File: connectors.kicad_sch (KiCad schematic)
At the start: 9 parts, among them J1 PRT-14417, J6 10152803-00011LF, J9 Conn_01x02, P1 TC2050-IDC

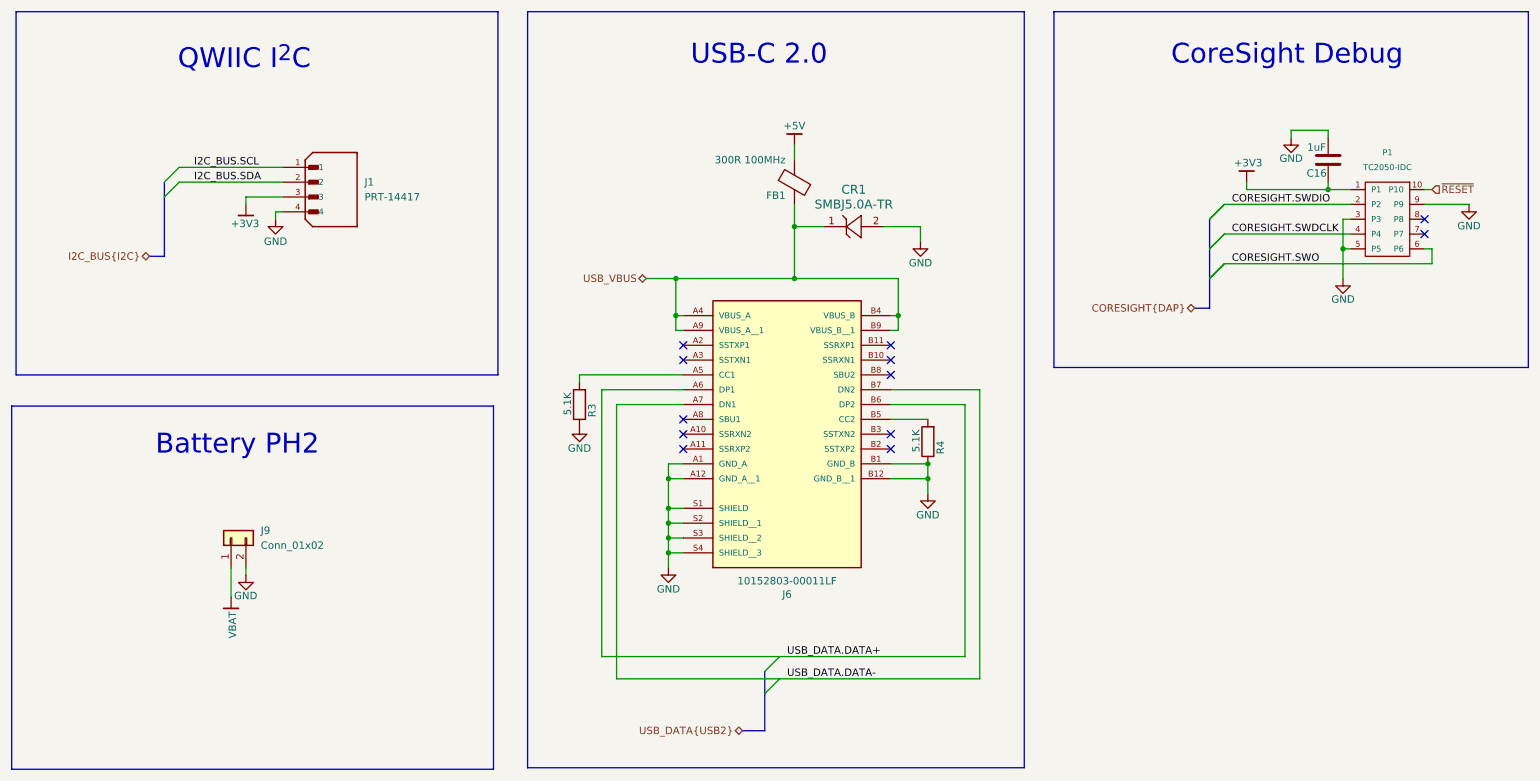
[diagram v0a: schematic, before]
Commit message: Release candidate
Changed USBC connector, changed TagConnect to use footprint with legs, move NRF52 to edge of board, clean up traces
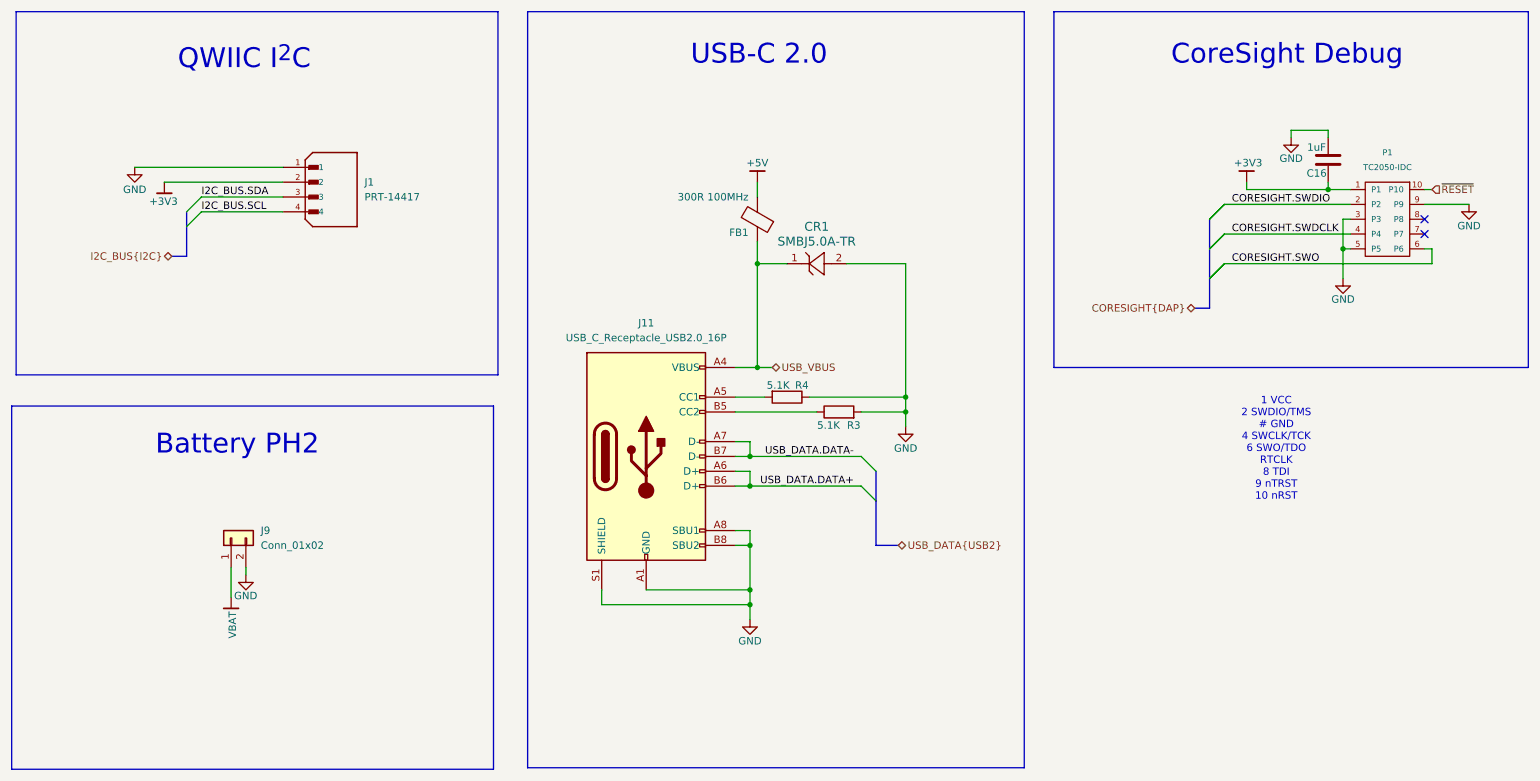
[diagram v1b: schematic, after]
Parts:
- removed J6: 10152803-00011LF, 10152803_00011LF:AMPHENOL_10152803-00011LF, symbol 10152803-00011LF:10152803-00011LF
- added J11: USB_C_Receptacle_USB2.0_16P, Connector_USB:USB_C_Receptacle_GCT_USB4105-xx-A_16P_TopMnt_Horizontal, symbol Connector:USB_C_Receptacle_USB2.0_16P
- P1: footprint Connector:Tag-Connect_TC2050-IDC-NL_2x05_P1.27mm_Vertical -> Connector:Tag-Connect_TC2050-IDC-FP_2x05_P1.27mm_Vertical
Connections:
- net +3V3: now also J1.2; no longer J1.3
- net GND: now also J1.1, R3.2, J11.A1 (GND), J11.A12 (GND), J11.A8 (SBU1), J11.B1 (GND), J11.B12 (GND), J11.B8 (SBU2), J11.S1 (SHIELD); no longer J1.4, R3.1
- net I2C_BUS.SCL: now also J1.4; no longer J1.1
- net I2C_BUS.SDA: now also J1.3; no longer J1.2
- net USB_DATA.DATA+: now also J11.A6 (D+), J11.B6 (D+)
- net USB_DATA.DATA-: now also J11.A7 (D-), J11.B7 (D-)
- net USB_VBUS: now also J11.A4 (VBUS), J11.A9 (VBUS), J11.B4 (VBUS), J11.B9 (VBUS)
- net at R4.2: now also J11.A5 (CC1)
- new net: J11.B5 (CC2), R3.1
- no-connect marks 12 -> 2
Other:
- note added: "1 VCC 2 SWDIO/TMS # GND 4 SWCLK/TCK 6 SWO/TDO RTCLK 8 TDI 9 nTRST 10 nRST"
- moved on the sheet: CR1, FB1, R3, R4

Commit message: Update part numbers
Update part numbers for 12 and 16 PIN SMD 2.54mm pins and USB-C 2.0 connector.
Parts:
- J11: MP (none) -> USB4105-GF-A
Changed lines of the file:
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@@
+			)
+		)
+		(property "MP" "USB4105-GF-A"
+			(at 128.27 93.98 0)
+			(effects
+				(font
+					(size 1.27 1.27)
+				)
+				(hide yes)
 			)
 		)

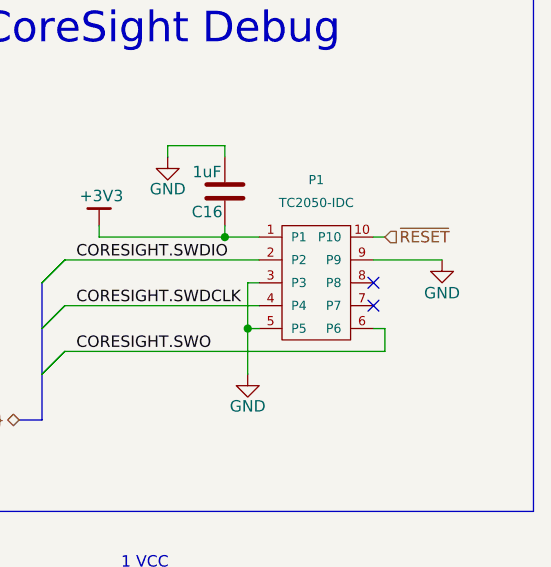
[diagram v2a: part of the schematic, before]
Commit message: Tweak locations and add a bypass capacitor for VBUS
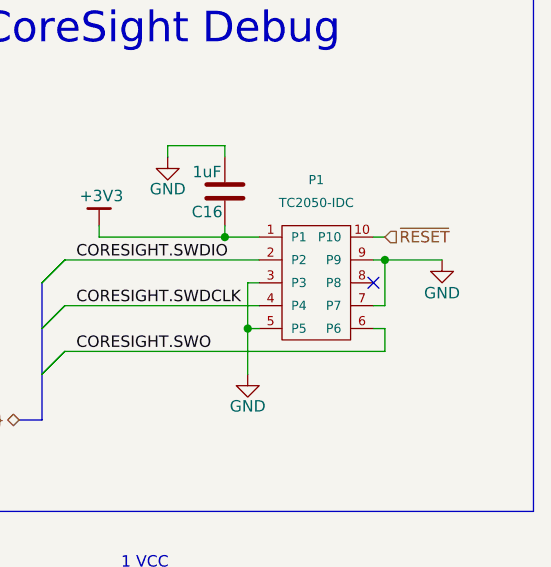
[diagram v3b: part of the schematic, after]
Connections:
- net GND: now also P1.7 (P7)
- no-connect marks 2 -> 1
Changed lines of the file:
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@@
+		(color 0 0 0 0)
+	)
+	(junction
+		(at 262.89 50.8)
+		(diameter 0)
 		(color 0 0 0 0)
 	)
@@
 		(at 261.62 53.34)
 	)
-	(no_connect
-		(at 261.62 55.88)
-	)
 	(bus_entry
 		(at 167.64 96.52)
@@
 	(wire
 		(pts
+			(xy 261.62 55.88) (xy 262.89 55.88)
+		)
+		(stroke
+			(width 0)
+			(type default)
+		)
+	)
+	(wire
+		(pts
 			(xy 231.14 48.26) (xy 231.14 46.99)
 		)
@@
 	(wire
 		(pts
+			(xy 262.89 50.8) (xy 261.62 50.8)
+		)
+		(stroke
+			(width 0)
+			(type default)
+		)
+	)
+	(wire
+		(pts
 			(xy 143.51 93.98) (xy 146.05 93.98)
 		)
@@
 	(wire
 		(pts
+			(xy 262.89 50.8) (xy 262.89 55.88)
+		)
+		(stroke
+			(width 0)
+			(type default)
+		)
+	)
+	(wire
+		(pts
 			(xy 245.11 48.26) (xy 248.92 48.26)
 		)
@@
 	(wire
 		(pts
-			(xy 269.24 50.8) (xy 261.62 50.8)
-		)
-		(stroke
+			(xy 269.24 50.8) (xy 262.89 50.8)
+		)
+		(stroke
